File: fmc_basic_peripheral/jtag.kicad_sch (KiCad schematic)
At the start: 8 parts, among them J5 Conn_JTAG_20, SW6 TL3342F160QG, U14 TXS02612RTWR

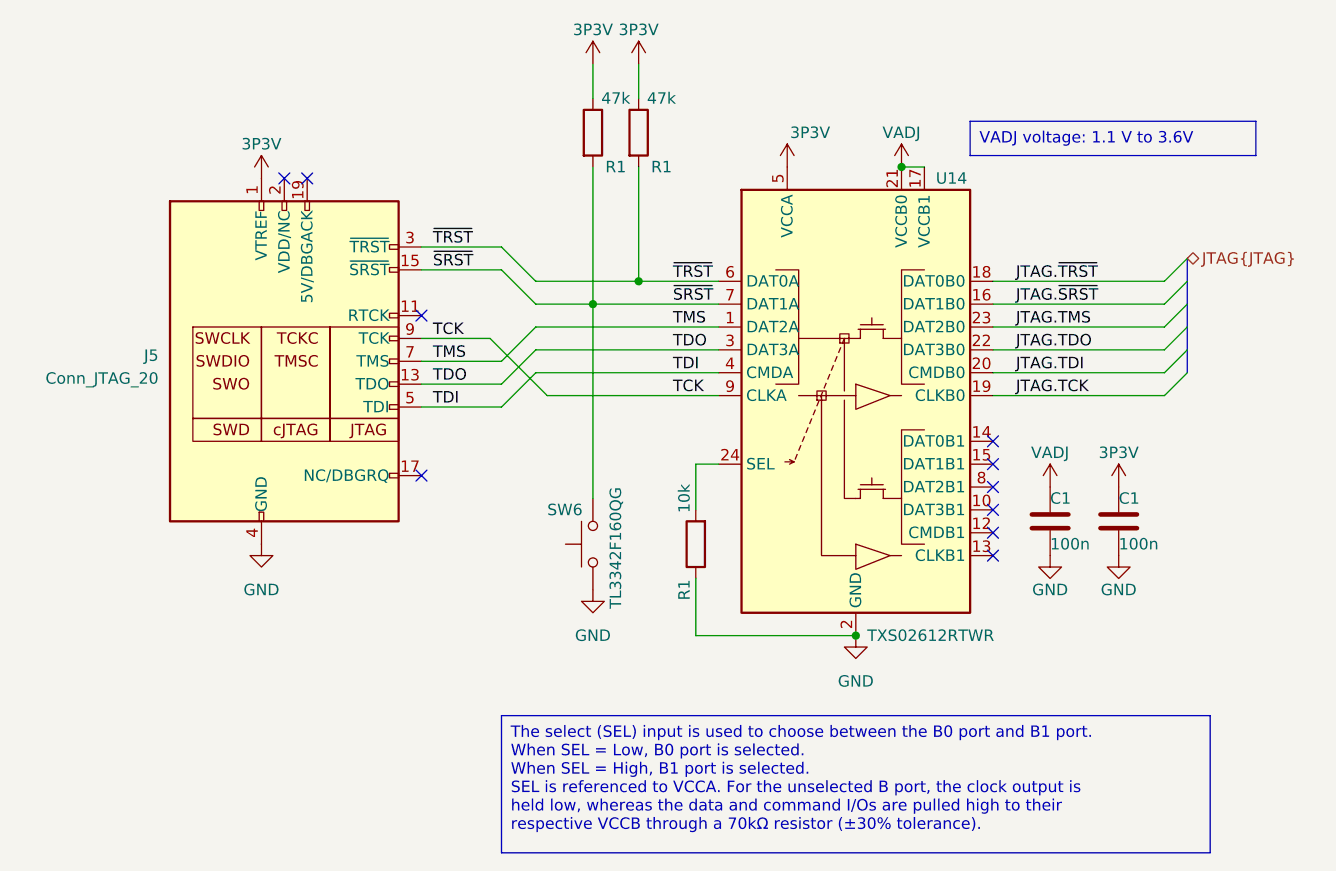
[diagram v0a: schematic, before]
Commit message: fmc_basic_peripheral: Migrate to kicad8
- Migrate schematics to kicad8
- Migrate PCB to kicad8
- Clean ERC
- Clean LVS and DRC

Signed-off-by: Huang Rui <vowstar@gmail.com>
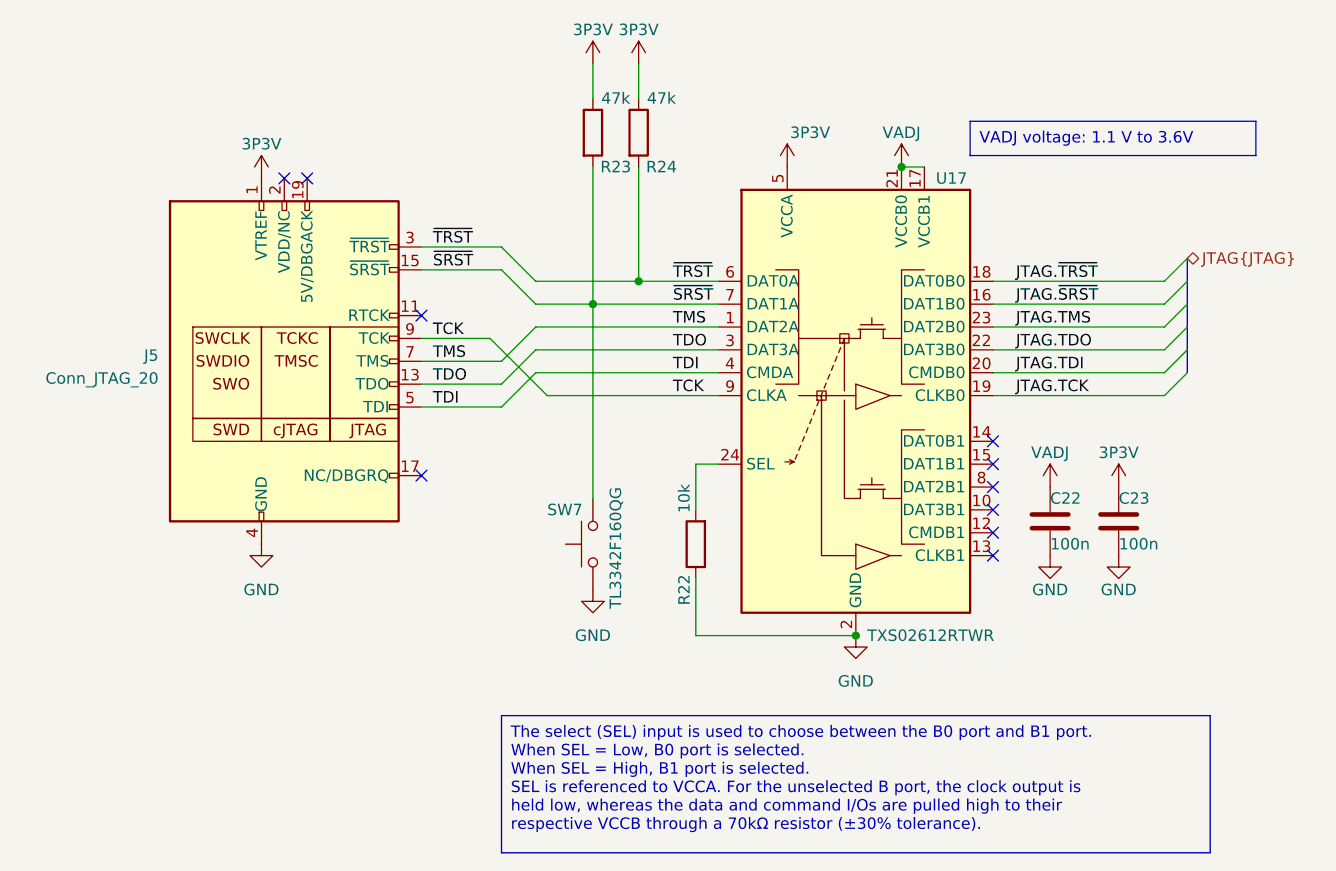
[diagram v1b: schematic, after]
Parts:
- renumbered C1 to C22, C1 to C23, R1 to R22, R1 to R23, R1 to R24, SW6 to SW7, U14 to U17
